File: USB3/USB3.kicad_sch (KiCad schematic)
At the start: 3 parts, among them U2 TUSB8041

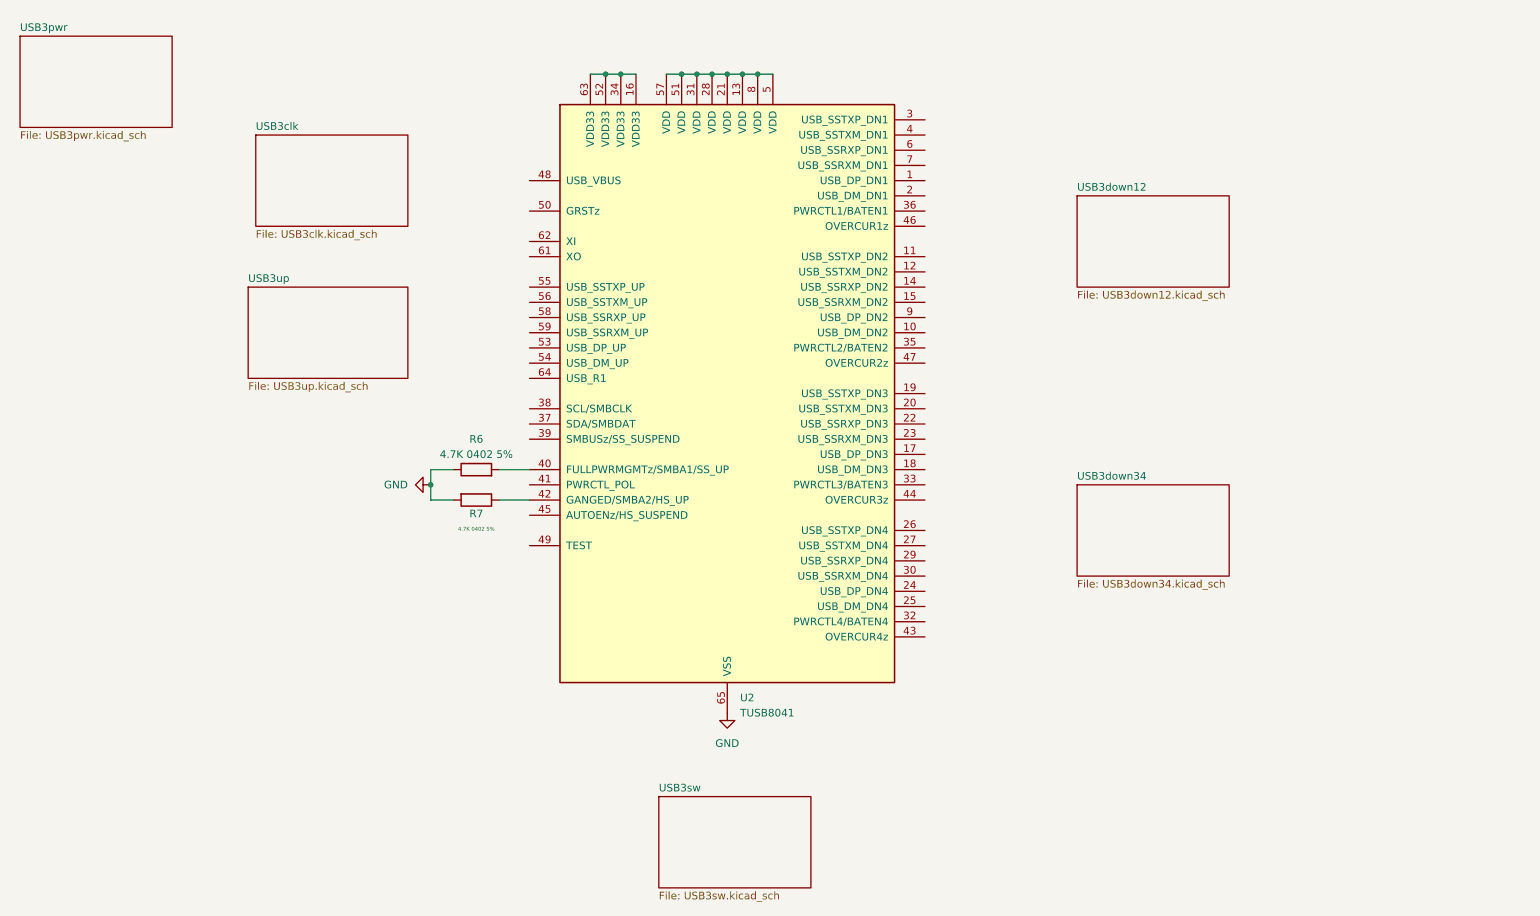
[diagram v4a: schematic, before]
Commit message: finished usb3.0
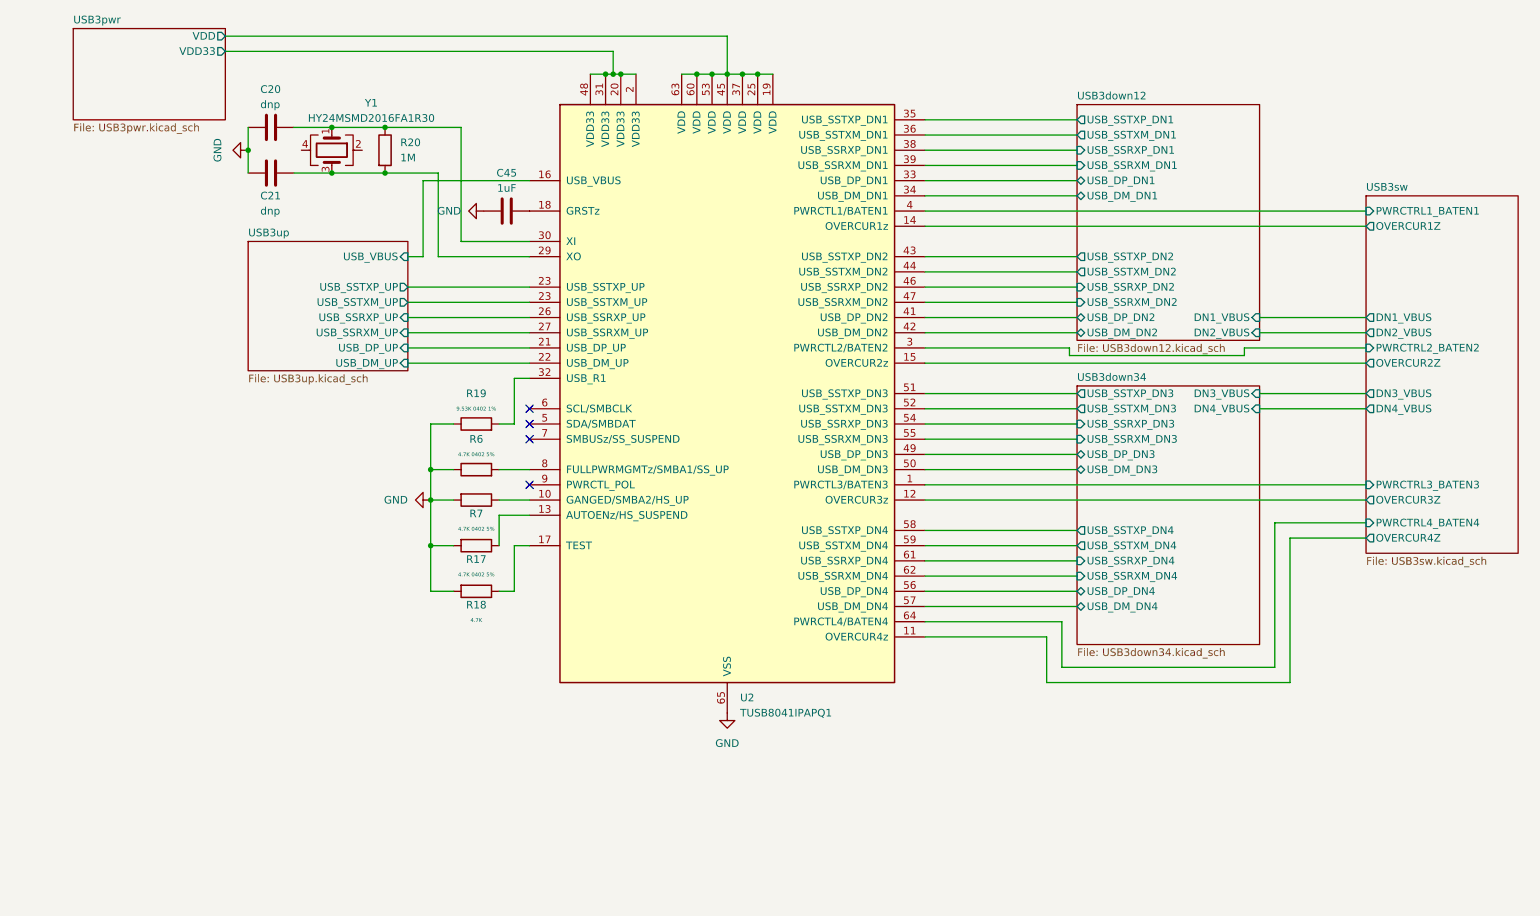
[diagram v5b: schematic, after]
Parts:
- added C20, C21: dnp, symbol Device:C
- added C45: 1uF, symbol Device:C
- added R17: 4.7K 0402 5%, symbol Device:R
- added R18: 4.7K, symbol Device:R
- added R19: 9.53K 0402 1%, symbol Device:R
- added R20: 1M, symbol Device:R
- added Y1: HY24MSMD2016FA1R30, symbol Device:Crystal_GND24
- U2: value TUSB8041 -> TUSB8041IPAPQ1
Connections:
- net GND: now also C20.2, C21.2, C45.2, R17.2, R18.2, R19.1
- net at R7.1: now also U2.10 (GANGED/SMBA2/HS_UP); no longer U2.42 (GANGED/SMBA2/HS_UP)
- net USB3sw/PWRCTRL3_BATEN3: now reaches U2.1 (PWRCTL3/BATEN3)
- net USB3sw/OVERCUR4Z: now reaches U2.11 (OVERCUR4z)
- net USB3sw/OVERCUR3Z: now reaches U2.12 (OVERCUR3z)
- net USB3sw/OVERCUR1Z: now reaches U2.14 (OVERCUR1z)
- net USB3sw/OVERCUR2Z: now reaches U2.15 (OVERCUR2z)
- net at U2.17 (TEST): now also R18.1
- net at U2.18 (GRSTz): now also C45.1
- net USB3pwr/VDD: now reaches U2.19 (VDD)
- net USB3pwr/VDD: now also U2.25 (VDD), U2.37 (VDD), U2.45 (VDD), U2.53 (VDD), U2.60 (NC), U2.63 (VDD)
- net USB3pwr/VDD33: now reaches U2.2 (VDD33)
- net USB3pwr/VDD33: now also U2.20 (VDD33), U2.31 (VDD33), U2.48 (VDD33)
- net USB3up/USB_DM_UP: now reaches U2.22 (USB_DM_UP)
- net USB3up/USB_SSTXP_UP: now reaches U2.23 (USB_SSTXM_UP)
- net USB3up/USB_SSRXP_UP: now reaches U2.26 (USB_SSRXP_UP)
- net USB3up/USB_SSRXM_UP: now reaches U2.27 (USB_SSRXM_UP)
- net at U2.29 (XO): now also C21.1, R20.2, Y1.3
- net USB3sw/PWRCTRL2_BATEN2: now reaches U2.3 (PWRCTL2/BATEN2)
- net at U2.30 (XI): now also C20.1, R20.1, Y1.1
- net at U2.32 (USB_R1): now also R19.2
- net USB3down12/USB_DP_DN1: now reaches U2.33 (USB_DP_DN1)
- net USB3down12/USB_SSTXP_DN1: now reaches U2.35 (USB_SSTXP_DN1)
- net USB3down12/USB_SSTXM_DN1: now reaches U2.36 (USB_SSTXM_DN1)
- net USB3down12/USB_SSRXP_DN1: now reaches U2.38 (USB_SSRXP_DN1)
- net USB3down12/USB_SSRXM_DN1: now reaches U2.39 (USB_SSRXM_DN1)
- net USB3sw/PWRCTRL1_BATEN1: now reaches U2.4 (PWRCTL1/BATEN1)
- net at R6.2: now also U2.8 (FULLPWRMGMTz/SMBA1/SS_UP); no longer U2.40 (FULLPWRMGMTz/SMBA1/SS_UP)
- net USB3down12/USB_DP_DN2: now reaches U2.41 (USB_DP_DN2)
- net USB3down12/USB_SSTXP_DN2: now reaches U2.43 (USB_SSTXP_DN2)
- net USB3down12/USB_SSTXM_DN2: now reaches U2.44 (USB_SSTXM_DN2)
- net USB3down12/USB_SSRXP_DN2: now reaches U2.46 (USB_SSRXP_DN2)
- net USB3down12/USB_SSRXM_DN2: now reaches U2.47 (USB_SSRXM_DN2)
- net USB3down34/USB_DP_DN3: now reaches U2.49 (USB_DP_DN3)
- net USB3down34/USB_DM_DN3: now reaches U2.50 (USB_DM_DN3)
- net USB3down34/USB_SSRXP_DN3: now reaches U2.54 (USB_SSRXP_DN3)
- net USB3down34/USB_SSRXM_DN3: now reaches U2.55 (USB_SSRXM_DN3)
- net USB3down34/USB_DP_DN4: now reaches U2.56 (USB_DP_DN4)
- net USB3down34/USB_SSTXP_DN4: now reaches U2.58 (USB_SSTXP_DN4)
- net USB3down34/USB_SSTXM_DN4: now reaches U2.59 (USB_SSTXM_DN4)
- net USB3down34/USB_SSRXP_DN4: now reaches U2.61 (USB_SSRXP_DN4)
- net USB3down34/USB_SSRXM_DN4: now reaches U2.62 (USB_SSRXM_DN4)
- net USB3sw/PWRCTRL4_BATEN4: now reaches U2.64 (PWRCTL4/BATEN4)
- new net: R17.1, U2.13 (AUTOENz/HS_SUSPEND)
- new net USB3down12/USB_DM_DN1: U2.34 (USB_DM_DN1)
- new net USB3down12/USB_DM_DN2: U2.42 (USB_DM_DN2)
- new net USB3down34/USB_DM_DN4: U2.57 (USB_DM_DN4)
- new net USB3down34/USB_SSTXM_DN3: U2.52 (USB_SSTXM_DN3)
- new net USB3down34/USB_SSTXP_DN3: U2.51 (USB_SSTXP_DN3)
- new net USB3up/USB_DP_UP: U2.21 (USB_DP_UP)
- new net USB3up/USB_SSTXM_UP: U2.23 (USB_SSTXM_UP)
- new net USB3up/USB_VBUS: U2.16 (USB_VBUS)
- now unconnected: U2.5 (VDD)
- no-connect marks 0 -> 4
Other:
- removed sheet USB3clk
- sheet USB3down12 ports: added DN1_VBUS, DN2_VBUS, USB_DM_DN1, USB_DM_DN2, USB_DP_DN1, USB_DP_DN2, USB_SSRXM_DN1, USB_SSRXM_DN2, USB_SSRXP_DN1, USB_SSRXP_DN2, USB_SSTXM_DN1, USB_SSTXM_DN2, USB_SSTXP_DN1, USB_SSTXP_DN2; removed none
- sheet USB3down34 ports: added DN3_VBUS, DN4_VBUS, USB_DM_DN3, USB_DM_DN4, USB_DP_DN3, USB_DP_DN4, USB_SSRXM_DN3, USB_SSRXM_DN4, USB_SSRXP_DN3, USB_SSRXP_DN4, USB_SSTXM_DN3, USB_SSTXM_DN4, USB_SSTXP_DN3, USB_SSTXP_DN4; removed none
- sheet USB3pwr ports: added VDD, VDD33; removed none
- sheet USB3sw ports: added DN1_VBUS, DN2_VBUS, DN3_VBUS, DN4_VBUS, OVERCUR1Z, OVERCUR2Z, OVERCUR3Z, OVERCUR4Z, PWRCTRL1_BATEN1, PWRCTRL2_BATEN2, PWRCTRL3_BATEN3, PWRCTRL4_BATEN4; removed none
- sheet USB3up ports: added USB_DM_UP, USB_DP_UP, USB_SSRXM_UP, USB_SSRXP_UP, USB_SSTXM_UP, USB_SSTXP_UP, USB_VBUS; removed none
